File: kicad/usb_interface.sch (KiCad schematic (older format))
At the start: 17 parts, among them U601 ISO7220CD, U602 ISO7220CD, U603 ISO7220CD, U604 ISO7220CD, U605 SN74ALVC244PWR

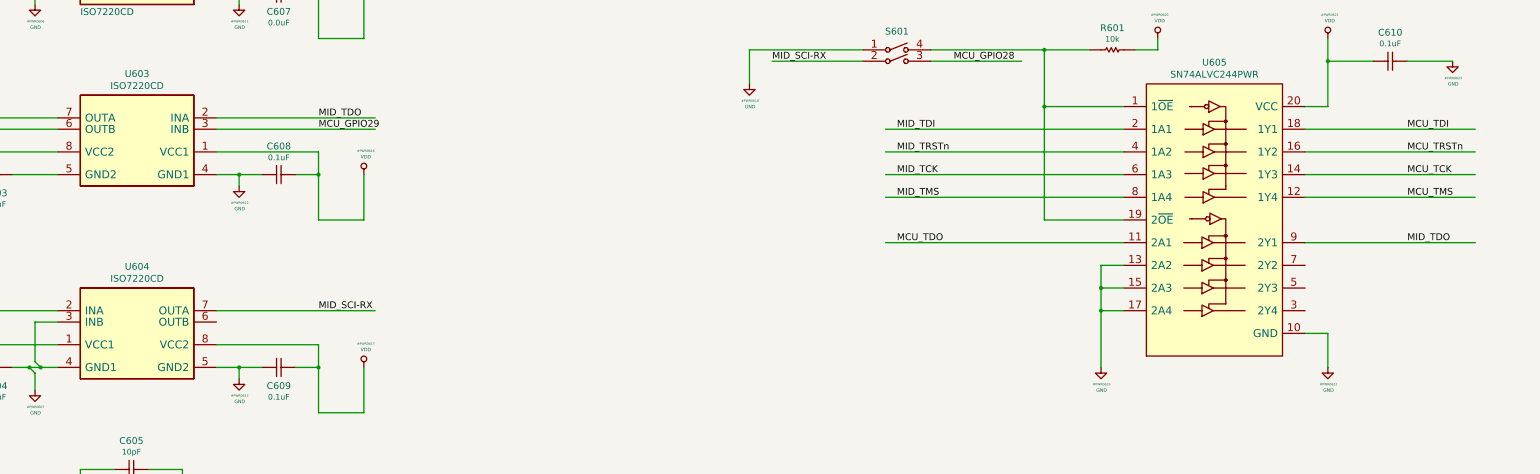
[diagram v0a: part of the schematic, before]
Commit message: datasheets added, I'll remove usb interface completely
I've decided to remove the jtag and isolation interface completely
maybe next I'll add some rs485 isolation interfase for debug, but for
now, it's not neccesary 'cose I'd use a jtag isolated interface
exclusively for that
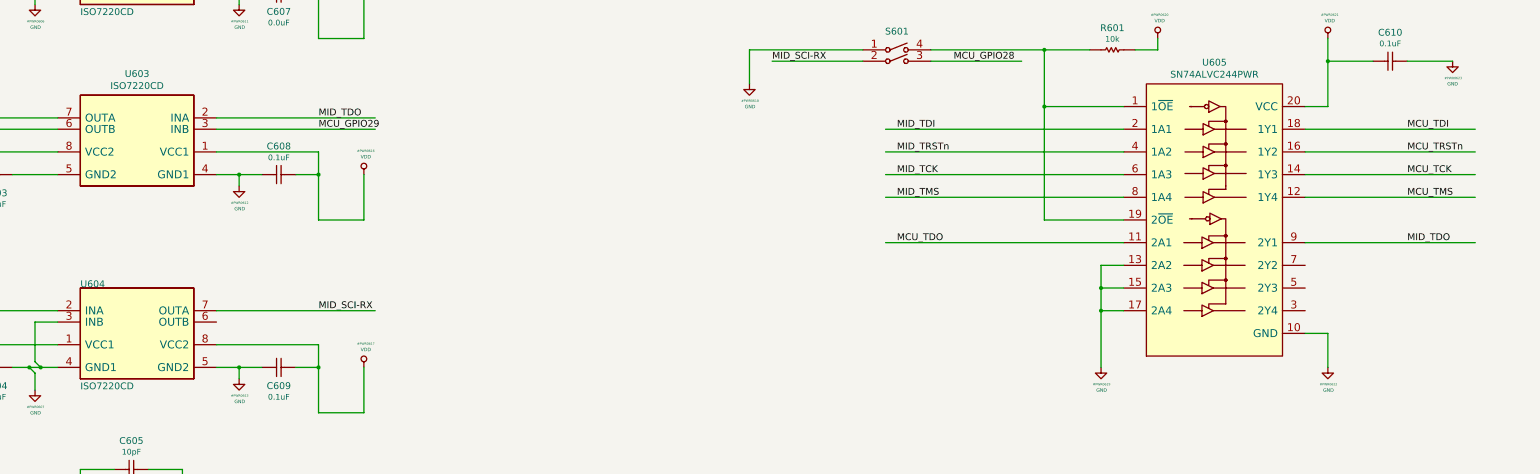
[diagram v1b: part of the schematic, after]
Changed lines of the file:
@@
 P 15000 4900
 F 0 "#PWR0623" H 15005 4751 20  0000 C CNN
-F 1 "GND" H 15005 4699 30  0000 C CNN
+F 1 "GND" H 15000 4700 30  0000 C CNN
 F 2 "" H 15000 4900 70  0000 C CNN
 F 3 "" H 15000 4900 70  0000 C CNN
@@
 F 1 "ISO7220CD" H 2900 3500 60  0000 L BNN
 F 2 "" H 2900 3500 60  0000 C CNN
-F 3 "" H 2900 3500 60  0000 C CNN
+F 3 "../doc/datasheets/iso7221c.pdf" H 2900 3500 60  0001 C CNN
 	1    3400 4000
 	1    0    0    -1
@@
 F 1 "ISO7220CD" H 3400 2883 60  0000 C CNN
 F 2 "" H 2900 1900 60  0000 C CNN
-F 3 "" H 2900 1900 60  0000 C CNN
+F 3 "../doc/datasheets/iso7221c.pdf" H 2900 1900 60  0001 C CNN
 	1    3400 2400
 	1    0    0    -1
@@
 U 1 1 5DB390ED
 P 3400 7300
-F 0 "U604" H 3400 7889 60  0000 C CNN
-F 1 "ISO7220CD" H 3400 7783 60  0000 C CNN
-F 2 "" H 2900 6800 60  0000 C CNN
-F 3 "" H 2900 6800 60  0000 C CNN
+F 0 "U604" H 2900 7700 60  0000 L BNN
+F 1 "ISO7220CD" H 2900 6800 60  0000 L BNN
+F 2 "" H 3400 7300 60  0001 C CNN
+F 3 "../doc/datasheets/iso7221c.pdf" H 3400 7300 60  0001 C CNN
 	1    3400 7300
 	1    0    0    -1
@@
 F 1 "ISO7220CD" H 3400 6083 60  0000 C CNN
 F 2 "" H 2900 5100 60  0000 C CNN
-F 3 "" H 2900 5100 60  0000 C CNN
+F 3 "../doc/datasheets/iso7221c.pdf" H 2900 5100 60  0001 C CNN
 	1    3400 5600
 	-1   0    0    -1
@@
 F 1 "SN74ALVC244PWR" H 12900 7583 60  0000 C CNN
 F 2 "" H 12300 5000 60  0000 C CNN
-F 3 "" H 12300 5000 60  0000 C CNN
+F 3 "../doc/datasheets/sn74alvc244.pdf" H 12300 5000 60  0001 C CNN
 	1    12900 6300
 	1    0    0    -1
